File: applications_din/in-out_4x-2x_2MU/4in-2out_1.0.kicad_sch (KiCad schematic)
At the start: 63 parts, among them IC1 ULN2803, J1 Con_CTRL, J2 Con_IO, J3 Con_230V, J4 Con_EIB_WAGO_243-211, J5 Con_230V, K1 HFE20-1/24-1HSD-L2, K2 HFE20-1/24-1HSD-L2, U1 74HC595, U2 74HC165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

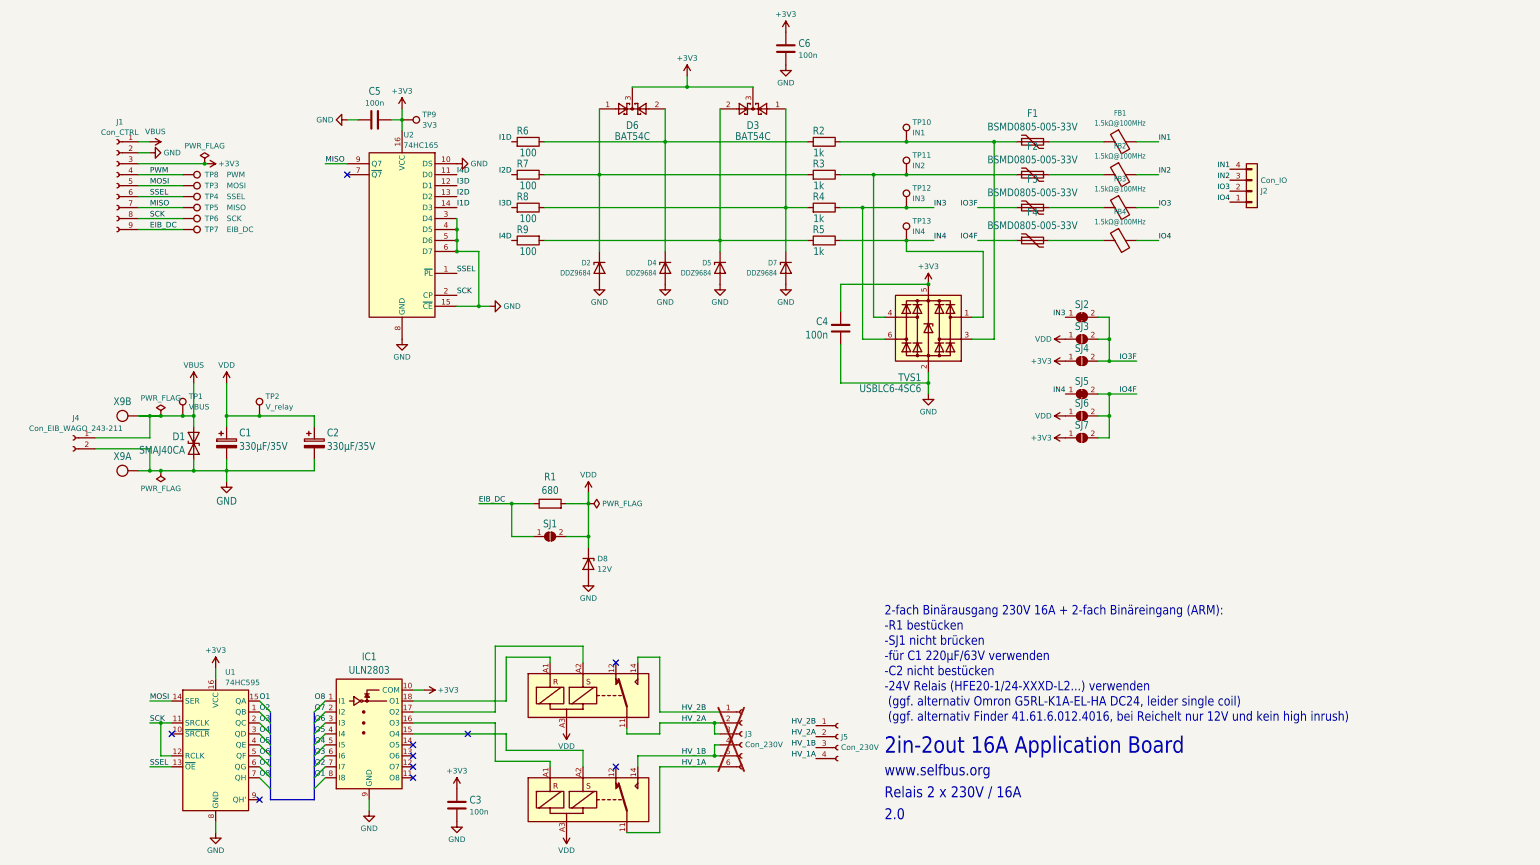
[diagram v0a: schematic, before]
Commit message: properly rename 4in-2out application & top projects
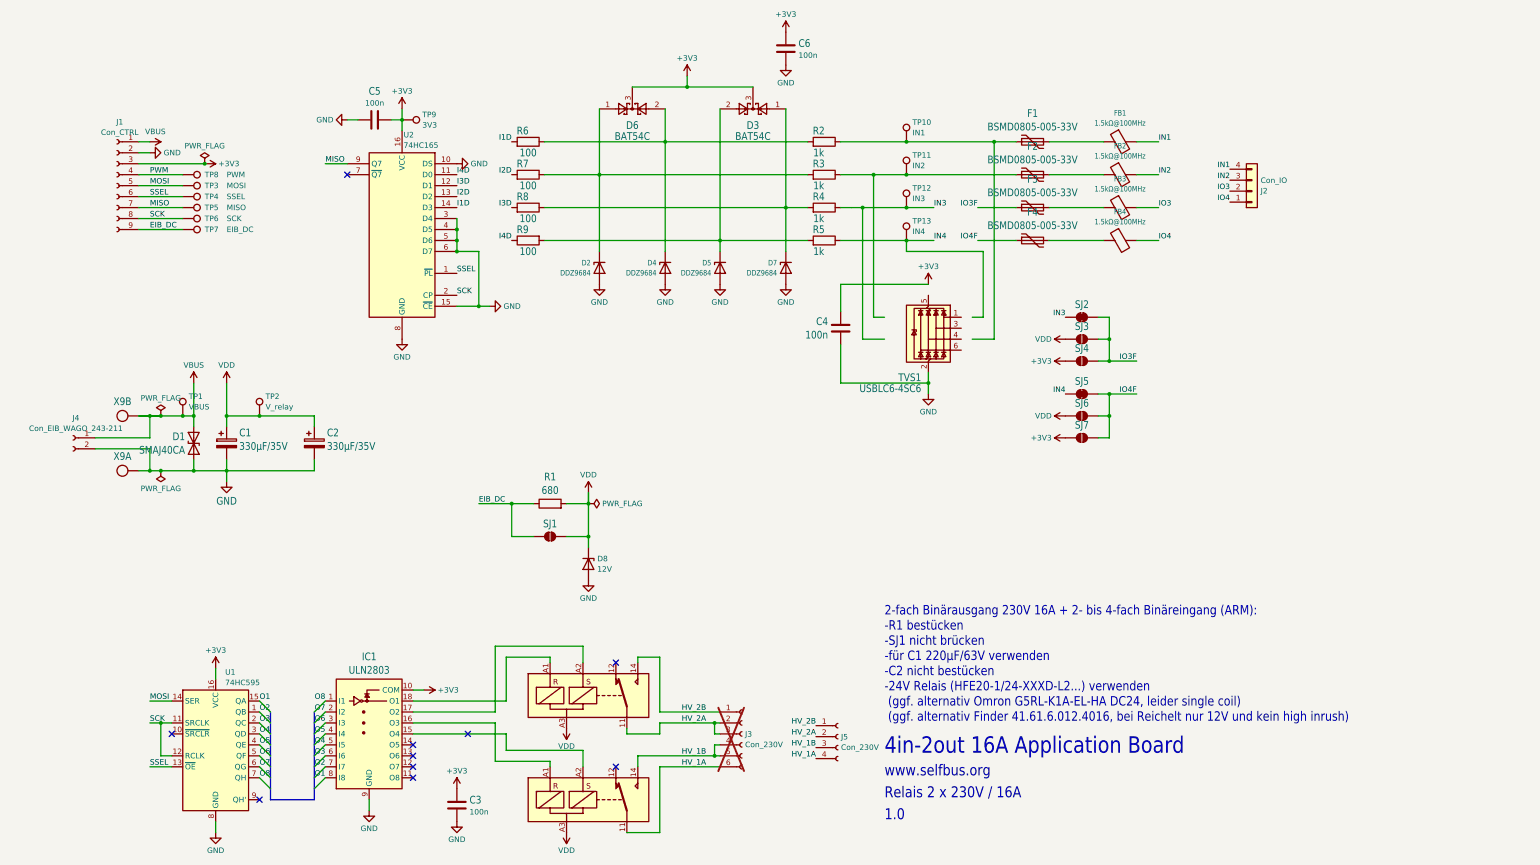
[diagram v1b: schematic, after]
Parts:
- K1, K2: footprint selfbus:HFE20-GENERIC-COMBO -> selfbus:HFE20-1-L2
- X9: footprint selfbus:W243-211_1x02_P5.75 -> selfbus:W237-102
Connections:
- net +3V3: no longer TVS1.5 (VBUS)
- net IN3: no longer TVS1.6 (I/O4)
- net IN4: no longer TVS1.1 (I/O1)
- net at F2.1, R3.1, TP11.1: no longer TVS1.4 (I/O3)
- net at F1.1, R2.1, TP10.1: no longer TVS1.3 (I/O2)
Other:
- note added: "1.0"
- note added: "2-fach Binärausgang 230V 16A + 2- bis 4-fach Binäreingang (ARM): -R1 bestücken -SJ1 nicht brücken -für C1 220µF/63V verwenden -C2 nicht bestücken -24V Relais (HFE20-1/24-XXXD-L2...) verwenden (ggf. alternativ Omron G5RL-K1A-EL-HA DC24, leider single coil) (ggf. alternativ Finder 41.61.6.012.4016, bei Reichelt nur 12V und kein high inrush)"
- note added: "4in-2out 16A Application Board"
- note removed: "2-fach Binärausgang 230V 16A + 2-fach Binäreingang (ARM): -R1 bestücken -SJ1 nicht brücken -für C1 220µF/63V verwenden -C2 nicht bestücken -24V Relais (HFE20-1/24-XXXD-L2...) verwenden (ggf. alternativ Omron G5RL-K1A-EL-HA DC24, leider single coil) (ggf. alternativ Finder 41.61.6.012.4016, bei Reichelt nur 12V und kein high inrush)"
- note removed: "2.0"
- note removed: "2in-2out 16A Application Board"

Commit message: update in-out_4x-2x_2MU - final for now
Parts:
- removed X9: W237-102, selfbus:W237-102, symbol selfbus:W237-102
- J4: value Con_EIB_WAGO_243-211 -> EIB_WAGO_243-211; footprint (none) -> selfbus:W243-211_1x02_P5.75
- K1, K2: footprint selfbus:HFE20-1-L2 -> selfbus:HFE20-GENERIC-COMBO
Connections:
- net +3V3: now also TVS1.5 (VBUS)
- net GND: now also J4.1 (Pin_1); no longer J4.2 (Pin_2)
- net IN3: now also TVS1.6 (I/O4)
- net IN4: now also TVS1.1 (I/O1)
- net VBUS: now also J4.2 (Pin_2); no longer J4.1 (Pin_1)
- net at F2.1, R3.1, TP11.1: now also TVS1.4 (I/O3)
- net at F1.1, R2.1, TP10.1: now also TVS1.3 (I/O2)
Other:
- moved on the sheet: C4, J4, TVS1
